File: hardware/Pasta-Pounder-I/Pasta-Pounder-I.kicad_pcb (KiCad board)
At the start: 2 copper layers, 54 parts, among them CN1 XT30UPB-M, J1 USB_C_Receptacle, J2 Brushed_Motor_1, J3 Brushed_Motor_2, J4 ESC_Port, J5 JST-SH, J6 ESC_Terminal, Q1 AO3401A, SW1 RESET-SW, SW2 BOOT-SW, SW3 5.8 ZSPT, U1 DRV8874PWPR, U2 DRV8874PWPR, U4 USBLC6-2P6, U5 ESP32S3W1, U7 SY8113BADC

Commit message: Initial PCB Movements
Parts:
- added REF**: MountingHole_3.2mm_M3_Pad, MountingHole:MountingHole_3.2mm_M3_Pad, F.Cu at (119.0, 121.0)
- added REF**: MountingHole_3.2mm_M3_Pad, MountingHole:MountingHole_3.2mm_M3_Pad, F.Cu at (119.0, 79.0)
- added REF**: MountingHole_3.2mm_M3_Pad, MountingHole:MountingHole_3.2mm_M3_Pad, F.Cu at (181.0, 121.0)
- added REF**: MountingHole_3.2mm_M3_Pad, MountingHole:MountingHole_3.2mm_M3_Pad, F.Cu at (181.0, 79.0)
- U5: footprint RF_Module:ESP32-S3-WROOM-1 -> lcsc_footprints:C3013946_WIRELM-SMD_ESP32-S3-WROOM-1U
- moved SW3 85.0 mm to (118.5, 86.8), turned to 180 degrees
- moved D2 80.9 mm to (128.0, 91.7), turned to -90 degrees
- moved C12 76.1 mm to (142.5, 113.5), turned to 180 degrees
- moved C27 73.8 mm to (127.9, 82.5)
- moved C28 73.7 mm to (127.9, 83.5)
- moved R12 72.7 mm to (131.6, 82.9)
- moved J1 70.8 mm to (140.0, 80.5), turned to 180 degrees
- moved L3 70.3 mm to (124.3, 83.1)
- moved J3 68.7 mm to (151.0, 121.0), turned to 90 degrees
- moved C14 68.4 mm to (126.5, 99.5), turned to 90 degrees
- moved C29 68.4 mm to (128.1, 86.6)
- moved R13 68.2 mm to (131.6, 84.5)
- moved C26 67.9 mm to (128.1, 85.0)
- moved U2 67.6 mm to (153.5, 113.0)
- moved R11 67.0 mm to (130.5, 91.7), turned to 90 degrees
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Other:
- board outline added: 70 x 50 mm

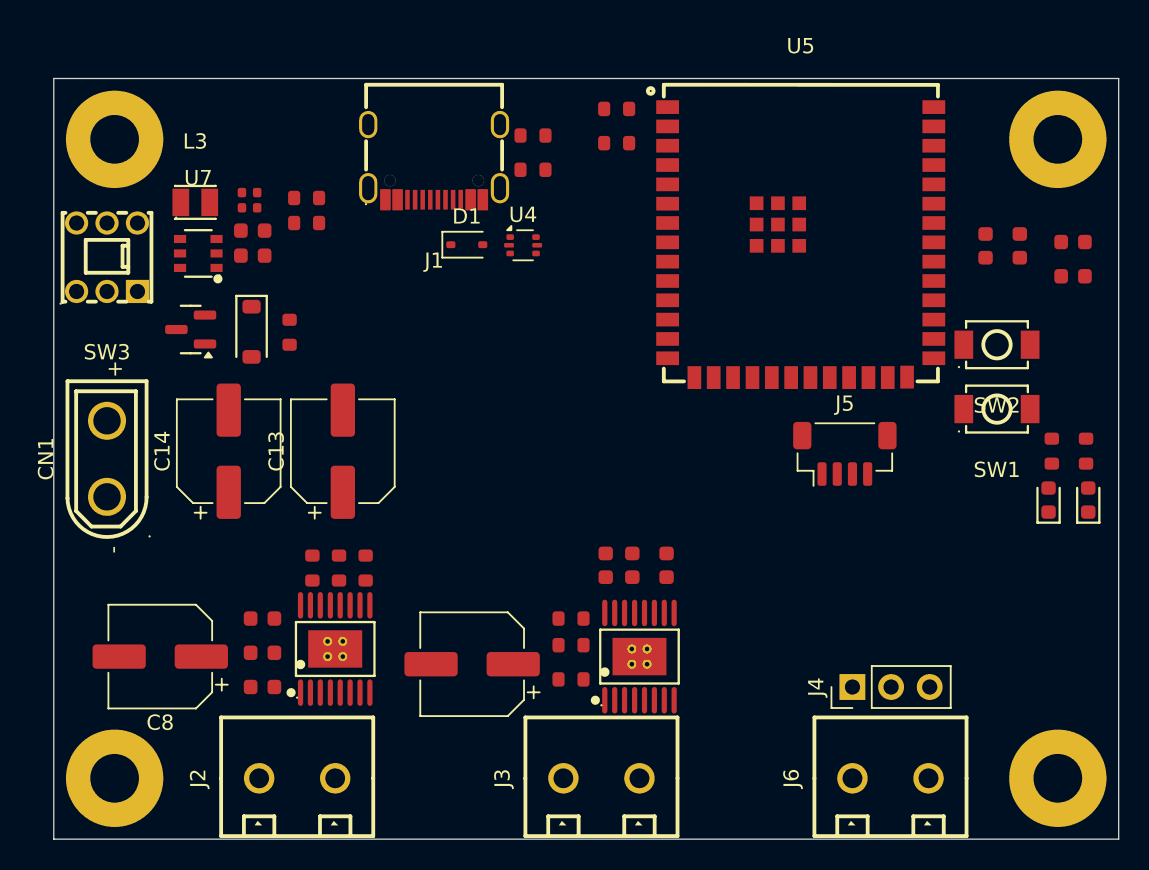
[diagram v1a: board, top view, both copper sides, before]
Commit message: Redid initial layout
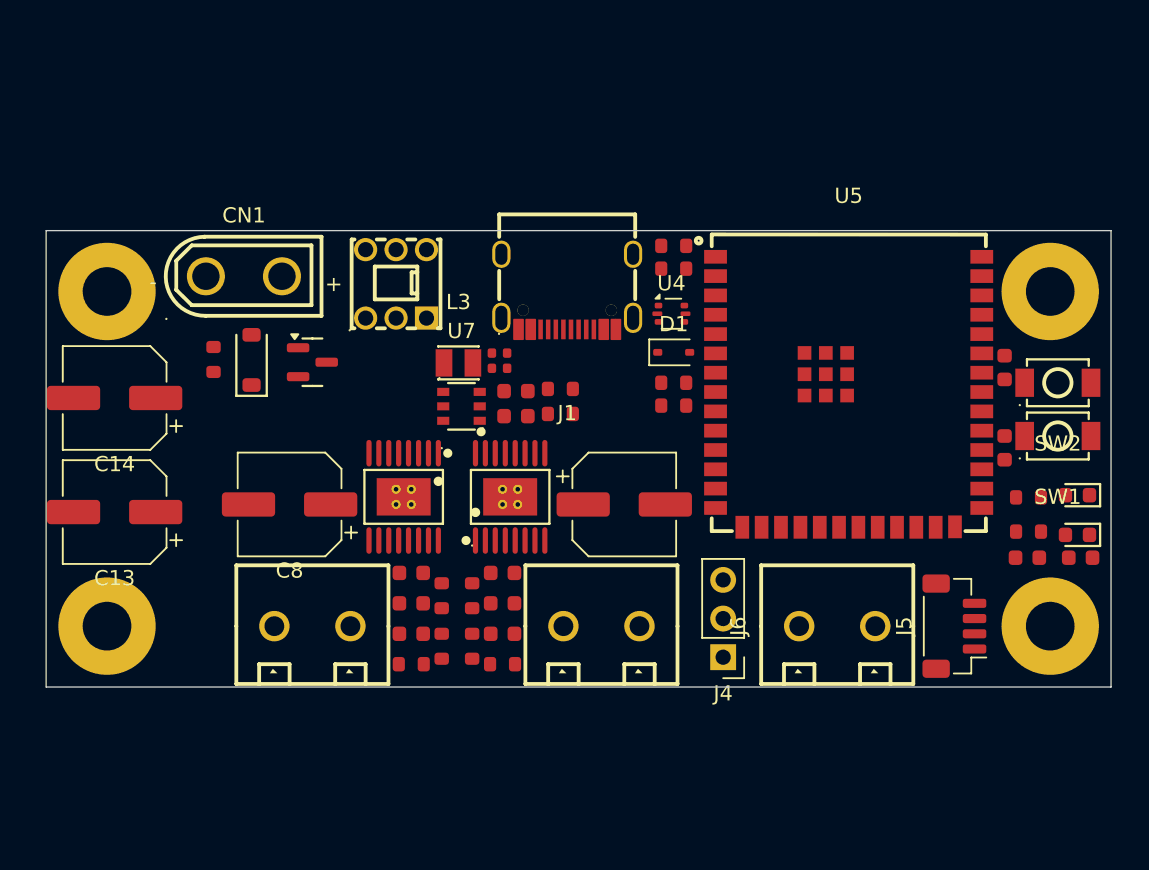
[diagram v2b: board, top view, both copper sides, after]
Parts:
- moved C1 21.0 mm to (179.0, 106.5)
- moved R12 20.9 mm to (148.3, 95.4)
- moved R13 20.9 mm to (148.3, 97.0)
- moved L3 20.3 mm to (141.6, 93.7)
- moved C26 20.3 mm to (145.4, 95.5)
- moved C29 20.3 mm to (145.4, 97.2)
- moved U7 20.0 mm to (141.8, 96.5)
- moved C27 19.5 mm to (144.3, 93.0)
- moved C28 19.5 mm to (144.3, 94.0)
- moved SW3 19.1 mm to (137.5, 88.5)
- moved C2 18.5 mm to (182.5, 106.5)
- moved R3 18.4 mm to (155.8, 95.0)
- moved R4 17.7 mm to (155.8, 96.5)
- moved C13 15.5 mm to (119.0, 103.5), turned to 180 degrees
- moved D1 15.3 mm to (155.8, 93.0)
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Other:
- board size 70 x 50 mm -> 70 x 30 mm

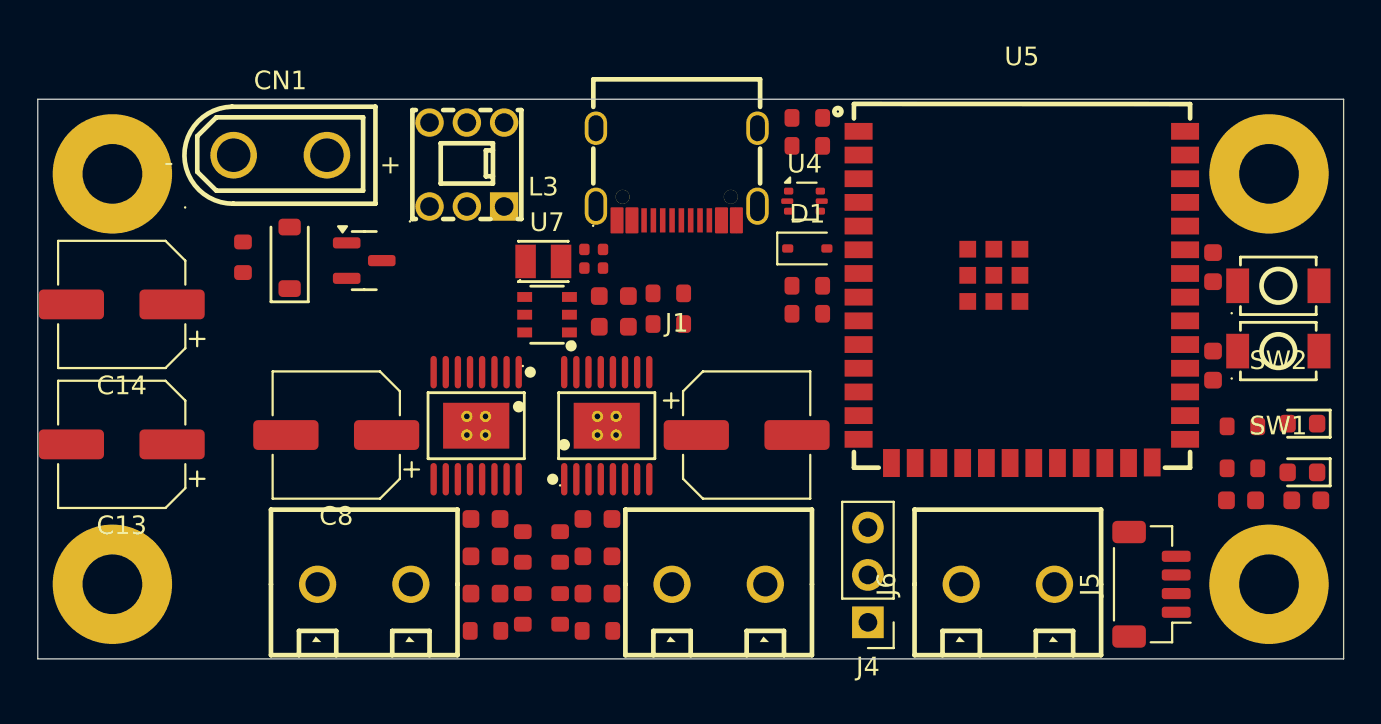
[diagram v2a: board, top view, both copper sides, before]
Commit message: Resized board to 70x25mm
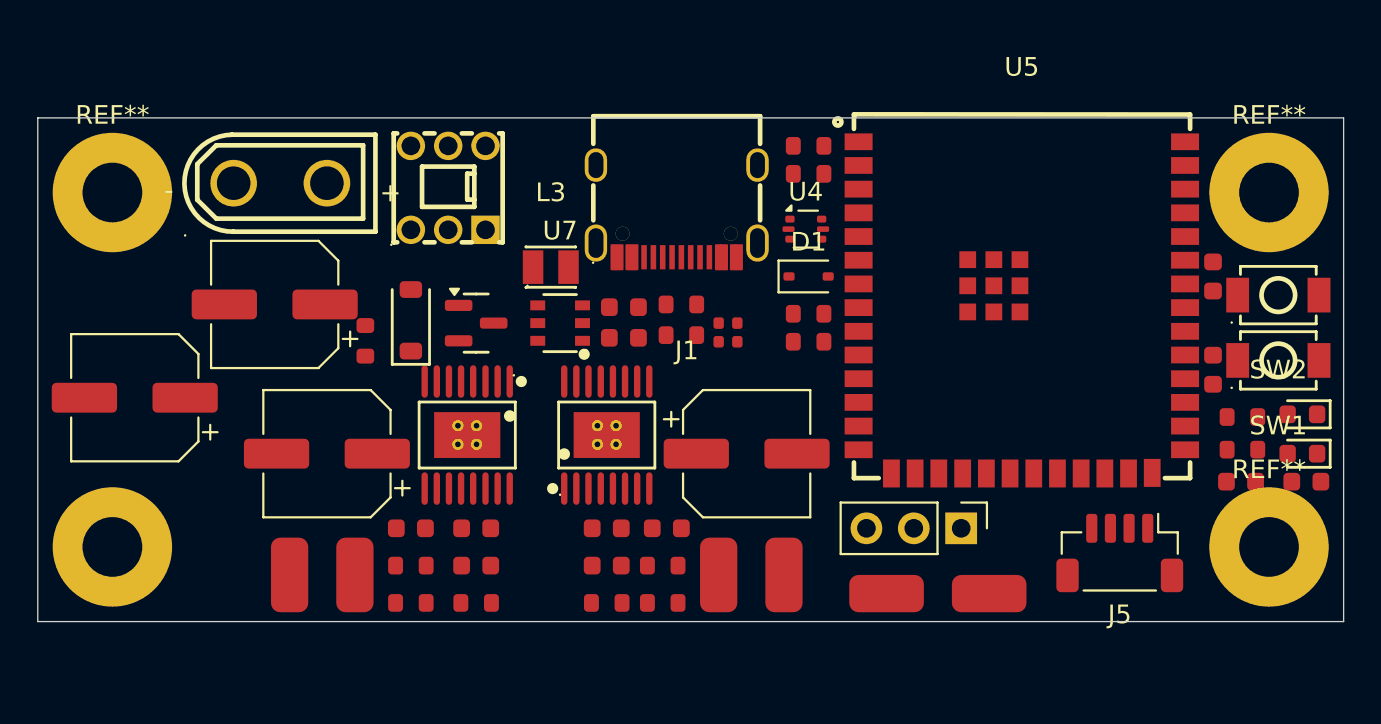
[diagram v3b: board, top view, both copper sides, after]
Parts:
- removed J2: Brushed_Motor_1, lcsc_footprints:C8404_CONN-TH_WJ126V-5_0-2P
- removed J3: Brushed_Motor_2, lcsc_footprints:C8404_CONN-TH_WJ126V-5_0-2P
- removed J6: ESC_Terminal, lcsc_footprints:C8404_CONN-TH_WJ126V-5_0-2P
- removed the REF** at (118.5, 111.0)
- removed the REF** at (118.5, 89.0)
- removed the REF** at (180.5, 111.0)
- removed the REF** at (180.5, 89.0)
- added J10: Motor_2-, Connector_Wire:SolderWirePad_1x01_SMD_2x4mm, F.Cu at (154.5, 110.5)
- added J11: ESC_VCC, Connector_Wire:SolderWirePad_1x01_SMD_2x4mm, F.Cu at (160.0, 111.5)
- added J12: ESC_GND, Connector_Wire:SolderWirePad_1x01_SMD_2x4mm, F.Cu at (165.5, 111.5)
- added J7: Motor_1+, Connector_Wire:SolderWirePad_1x01_SMD_2x4mm, F.Cu at (128.0, 110.5)
- added J8: Motor_1-, Connector_Wire:SolderWirePad_1x01_SMD_2x4mm, F.Cu at (131.5, 110.5)
- added J9: Motor_2+, Connector_Wire:SolderWirePad_1x01_SMD_2x4mm, F.Cu at (151.0, 110.5)
- added REF**: MountingHole_3.2mm_M3_Pad, MountingHole:MountingHole_3.2mm_M3_Pad, F.Cu at (180.5, 90.0)
- added REF**: MountingHole_3.2mm_M3_Pad, MountingHole:MountingHole_3.2mm_M3_Pad, F.Cu at (118.5, 90.0)
- added REF**: MountingHole_3.2mm_M3_Pad, MountingHole:MountingHole_3.2mm_M3_Pad, F.Cu at (118.5, 109.0)
- added REF**: MountingHole_3.2mm_M3_Pad, MountingHole:MountingHole_3.2mm_M3_Pad, F.Cu at (180.5, 109.0)
- moved C13 11.1 mm to (127.2, 96.0)
- moved C27 8.21 mm to (151.5, 97.0)
- moved C28 8.21 mm to (151.5, 98.0)
- moved R11 7.94 mm to (132.1, 98.0)
- moved D2 7.31 mm to (134.5, 96.8)
- moved J4 7.10 mm to (164.0, 108.0), turned to -90 degrees
- moved Q1 6.87 mm to (138.0, 97.0)
- moved R6 6.71 mm to (134.5, 112.0), turned to 180 degrees
- moved R7 6.43 mm to (134.5, 110.0), turned to 180 degrees
- moved R10 5.59 mm to (148.0, 110.0), turned to 0 degrees
- moved R9 5.51 mm to (148.0, 112.0), turned to 0 degrees
- moved C14 5.05 mm to (119.7, 101.0)
- moved C5 4.03 mm to (134.5, 108.0)
- moved C11 3.75 mm to (148.2, 108.0)
- moved J5 2.39 mm to (172.5, 109.3), turned to 180 degrees
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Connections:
- U1 pad 10: Net-(J2-Pin_1) -> M1-
- U1 pad 8: Net-(J2-Pin_2) -> M1+
- U2 pad 10: Net-(J3-Pin_1) -> M2-
- U2 pad 8: Net-(J3-Pin_2) -> M2+
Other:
- board size 70 x 30 mm -> 70 x 27 mm

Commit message: L Shaped Initial Movements
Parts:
- removed J10: Motor_2-, Connector_Wire:SolderWirePad_1x01_SMD_2x4mm
- removed J11: ESC_VCC, Connector_Wire:SolderWirePad_1x01_SMD_2x4mm
- removed J12: ESC_GND, Connector_Wire:SolderWirePad_1x01_SMD_2x4mm
- removed J7: Motor_1+, Connector_Wire:SolderWirePad_1x01_SMD_2x4mm
- removed J8: Motor_1-, Connector_Wire:SolderWirePad_1x01_SMD_2x4mm
- removed J9: Motor_2+, Connector_Wire:SolderWirePad_1x01_SMD_2x4mm
- added J2: Motor_Terminal_1, lcsc_footprints:C8404_CONN-TH_WJ126V-5_0-2P, F.Cu at (216.0, 72.5)
- added J3: Motor_Terminal_3, lcsc_footprints:C8404_CONN-TH_WJ126V-5_0-2P, F.Cu at (233.0, 72.5)
- added J6: ESC Terminal, lcsc_footprints:C8404_CONN-TH_WJ126V-5_0-2P, F.Cu at (199.0, 72.5)
- moved C8 95.1 mm to (216.5, 64.5)
- moved C12 89.4 mm to (232.7, 64.5)
- moved U2 87.9 mm to (225.0, 66.5)
- moved C10 86.3 mm to (223.2, 71.5)
- moved C11 86.3 mm to (226.4, 71.5)
- moved C9 86.3 mm to (223.2, 73.5)
- moved R10 86.3 mm to (226.2, 73.5)
- moved R8 86.3 mm to (223.2, 75.5)
- moved R9 86.3 mm to (226.2, 75.5)
- moved C5 80.3 mm to (206.0, 71.5)
- moved C6 80.3 mm to (209.5, 71.5)
- moved C7 80.3 mm to (209.5, 73.5)
- moved R5 80.3 mm to (209.5, 75.5)
- moved R6 80.3 mm to (206.0, 75.5)
- moved R7 80.3 mm to (206.0, 73.5)
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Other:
- board size 70 x 27 mm -> 123.5 x 71.5 mm
